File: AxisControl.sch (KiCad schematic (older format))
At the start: 2 parts, among them J14 Max, J15 Min

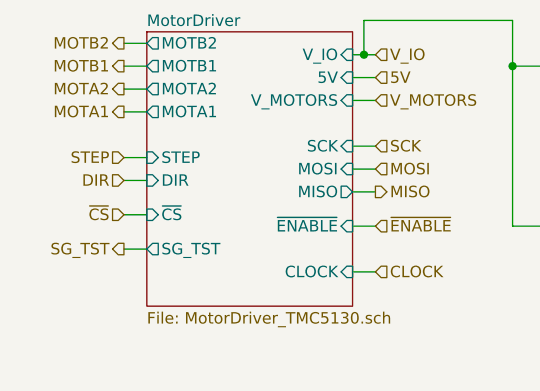
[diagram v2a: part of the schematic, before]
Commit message: Some useless changes, I'll remove the SD_MODE wire soon.
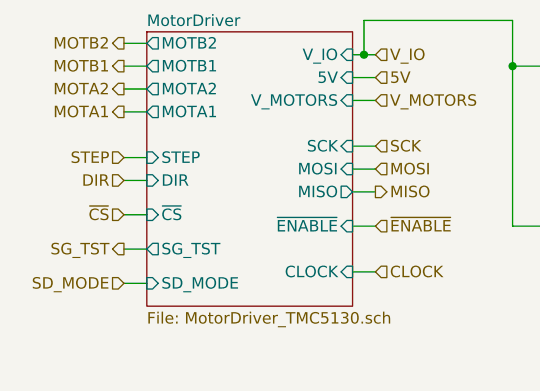
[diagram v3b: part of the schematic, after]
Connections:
- net labels added: SD_MODE
- wire segments 31 -> 32
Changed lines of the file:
@@
 F16 "MOTA2" O L 3550 3400 50
 F17 "MOTB2" O L 3550 3200 50
+F18 "SD_MODE" I L 3550 4250 50
 $EndSheet
 Text HLabel 3450 3500 0    50   Output ~ 0
@@
 Wire Wire Line
 	4550 4200 4450 4200
+Text HLabel 3450 4250 0    50   Input ~ 0
+SD_MODE
+Wire Wire Line
+	3450 4250 3550 4250
 $EndSCHEMATC

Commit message: Removed SD_MODE wire. Added motor clock oscillator. Wired the clock on the internal layer to reduce EMI.
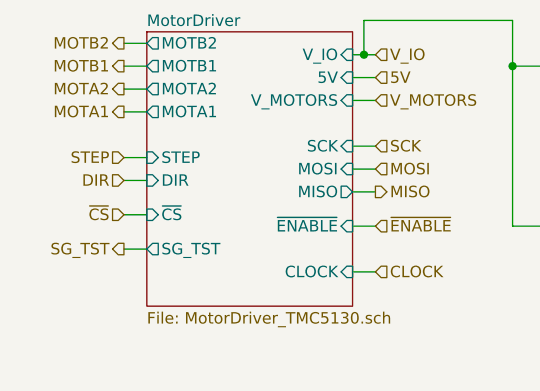
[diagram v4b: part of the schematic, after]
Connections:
- net labels removed: SD_MODE
- wire segments 32 -> 31
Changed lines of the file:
@@
 $Descr A4 11693 8268
 encoding utf-8
-Sheet 12 34
+Sheet 16 34
 Title ""
 Date ""
@@
 F16 "MOTA2" O L 3550 3400 50
 F17 "MOTB2" O L 3550 3200 50
-F18 "SD_MODE" I L 3550 4250 50
 $EndSheet
 Text HLabel 3450 3500 0    50   Output ~ 0
@@
 Wire Wire Line
 	4550 4200 4450 4200
-Text HLabel 3450 4250 0    50   Input ~ 0
-SD_MODE
-Wire Wire Line
-	3450 4250 3550 4250
 $EndSCHEMATC

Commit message: Updated schematics with the latest features.
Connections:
- net labels removed: 5V
- wire segments 31 -> 30
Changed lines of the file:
@@
 U 5ACC0B66
 F0 "MotorDriver" 50
-F1 "MotorDriver_TMC5130.sch" 50
+F1 "MotorDriver_TMC2660.sch" 50
 F2 "V_IO" I R 4450 3250 50
 F3 "V_MOTORS" I R 4450 3450 50
@@
 F10 "~ENABLE" I R 4450 4000 50
 F11 "SG_TST" O L 3550 4100 50
-F12 "5V" I R 4450 3350 50
-F13 "CLOCK" I R 4450 4200 50
-F14 "MOTB1" O L 3550 3300 50
-F15 "MOTA1" O L 3550 3500 50
-F16 "MOTA2" O L 3550 3400 50
-F17 "MOTB2" O L 3550 3200 50
+F12 "CLOCK" I R 4450 4200 50
+F13 "MOTB1" O L 3550 3300 50
+F14 "MOTA1" O L 3550 3500 50
+F15 "MOTA2" O L 3550 3400 50
+F16 "MOTB2" O L 3550 3200 50
 $EndSheet
 Text HLabel 3450 3500 0    50   Output ~ 0
@@
 Wire Wire Line
 	6250 3350 6050 3350
-Text HLabel 4550 3350 2    50   Input ~ 0
-5V
-Wire Wire Line
-	4550 3350 4450 3350
 Text HLabel 4550 4200 2    50   Input ~ 0
 CLOCK
